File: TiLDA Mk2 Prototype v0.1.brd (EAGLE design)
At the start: 68 x 100 mm, 215 parts, among them IC1 ATSAM3X8EA-AU, IC2 MPU-6050, IC3 SRF-V1.2, IC4 LTC4160, IC5 S25FL216K0PMFI011, IC6 AT45DB161E-SSHFHA (NP), IC7 HMC5883LSMD (NP), IC8 MCP1825T-3302E/DC, J1 ZX62-AB-5PA(11), J2 FCI 62684-401100ALF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

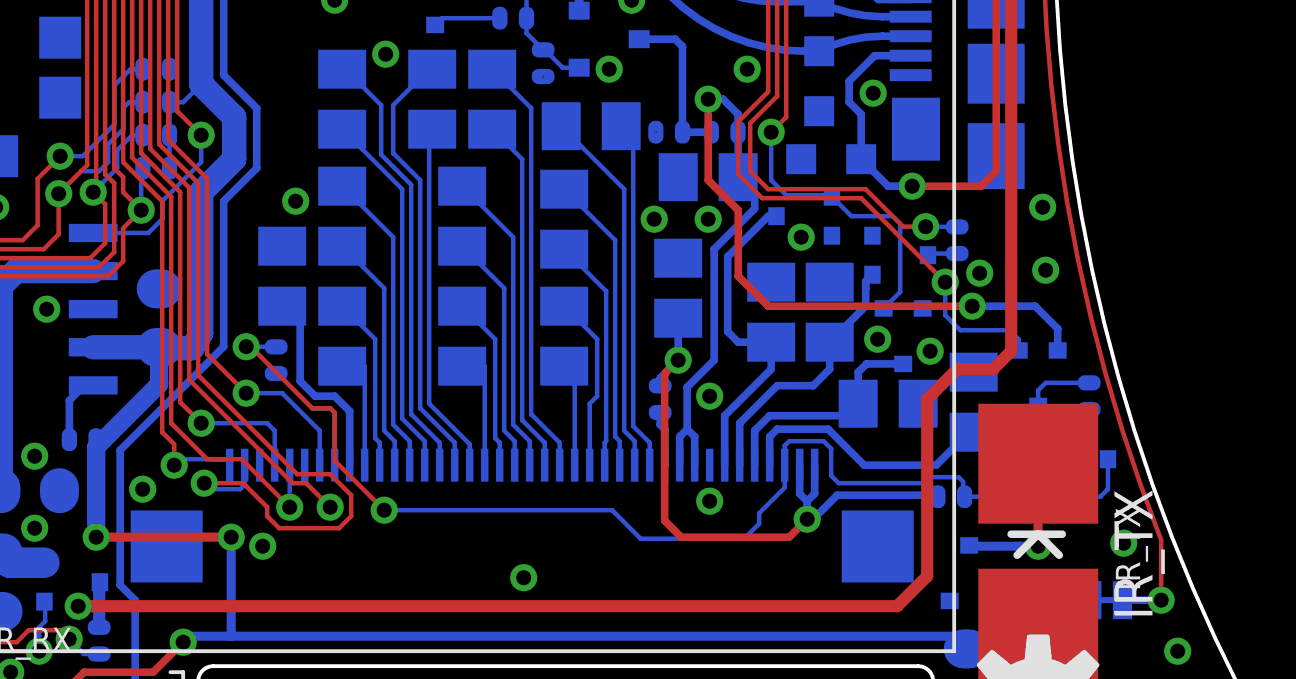
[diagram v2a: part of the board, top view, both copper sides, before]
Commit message: Prototype: C34, C38 to 10v, C21, C24, C25 to 0603 X5R
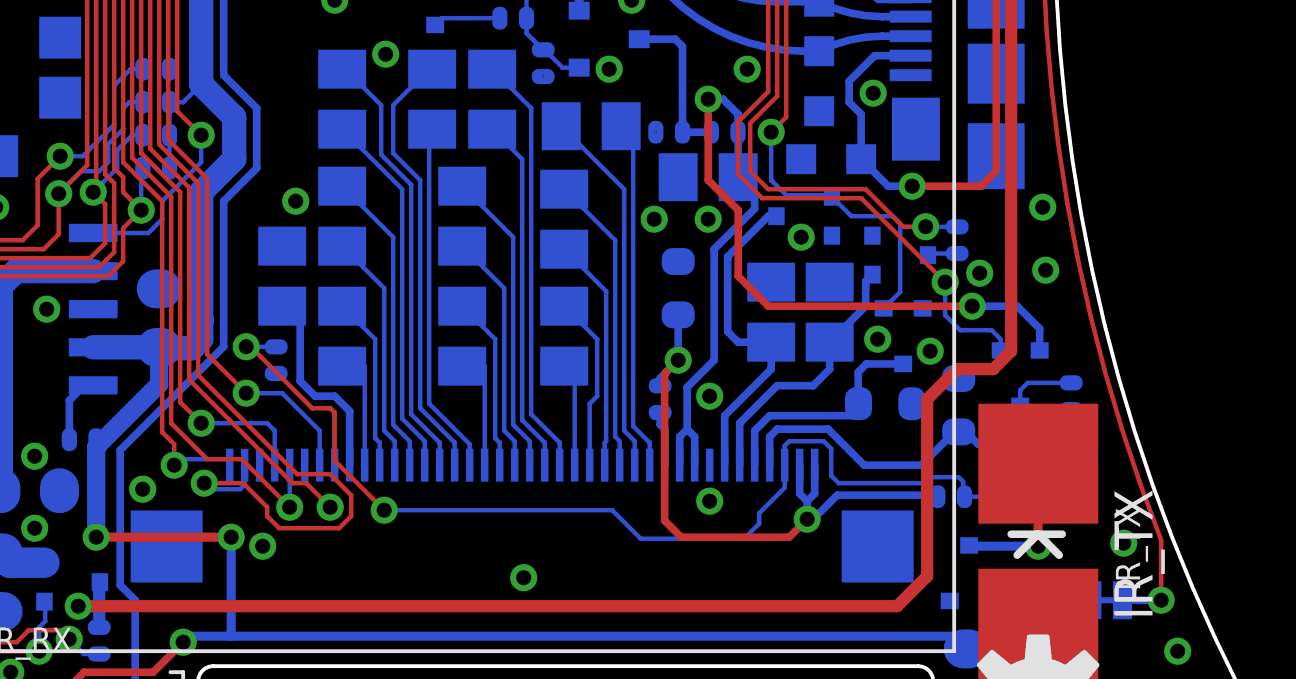
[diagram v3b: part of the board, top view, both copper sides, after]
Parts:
- C21, C24, C25: value 0805/1u/10V/X7R -> 0603/1u/10V/X5R; device TiLDA Mk2 Parts:C0805K -> TiLDA Mk2 Parts:C0603-ROUND
- C34, C38: value 0603/1u/6V/X5R -> 0603/1u/10V/X5R
- moved Q6 0.60 mm to (60.3, 10.9)
- moved Q7 0.60 mm to (58.9, 13.6)
- moved R10 0.60 mm to (58.4, 10.9)
- moved R12 0.60 mm to (60.6, 13.0)
- moved C25 0.51 mm to (56.9, 12.7)
- moved C24 0.10 mm to (54.4, 12.8)
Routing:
- net EPD_BORDER_CONTROL: track 65.8 -> 65.2 mm
- net EPD_VCC: track 33.9 -> 33.3 mm
- net BORDER: track 38.5 -> 37.9 mm
- net VDL: track 11.9 -> 11.3 mm

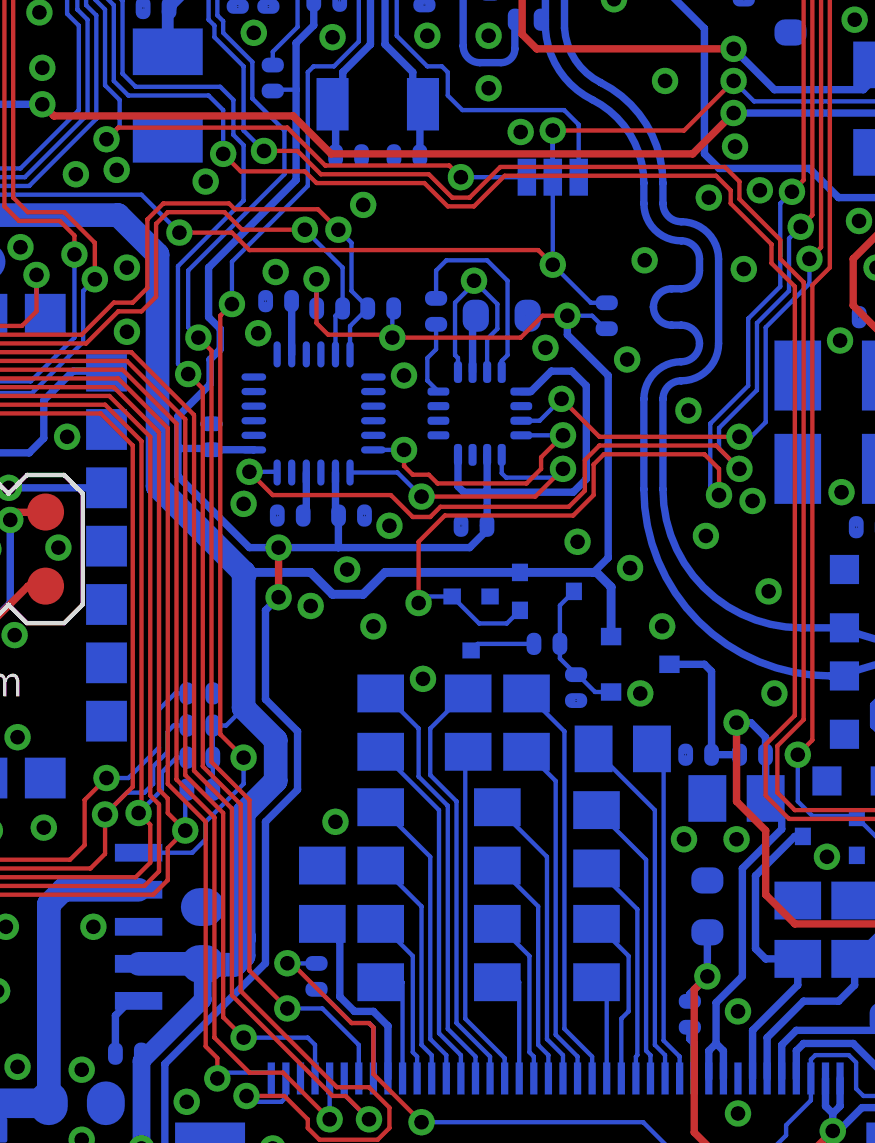
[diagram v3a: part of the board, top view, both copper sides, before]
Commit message: Prototype: Move C120 to NTRSB and VBackup
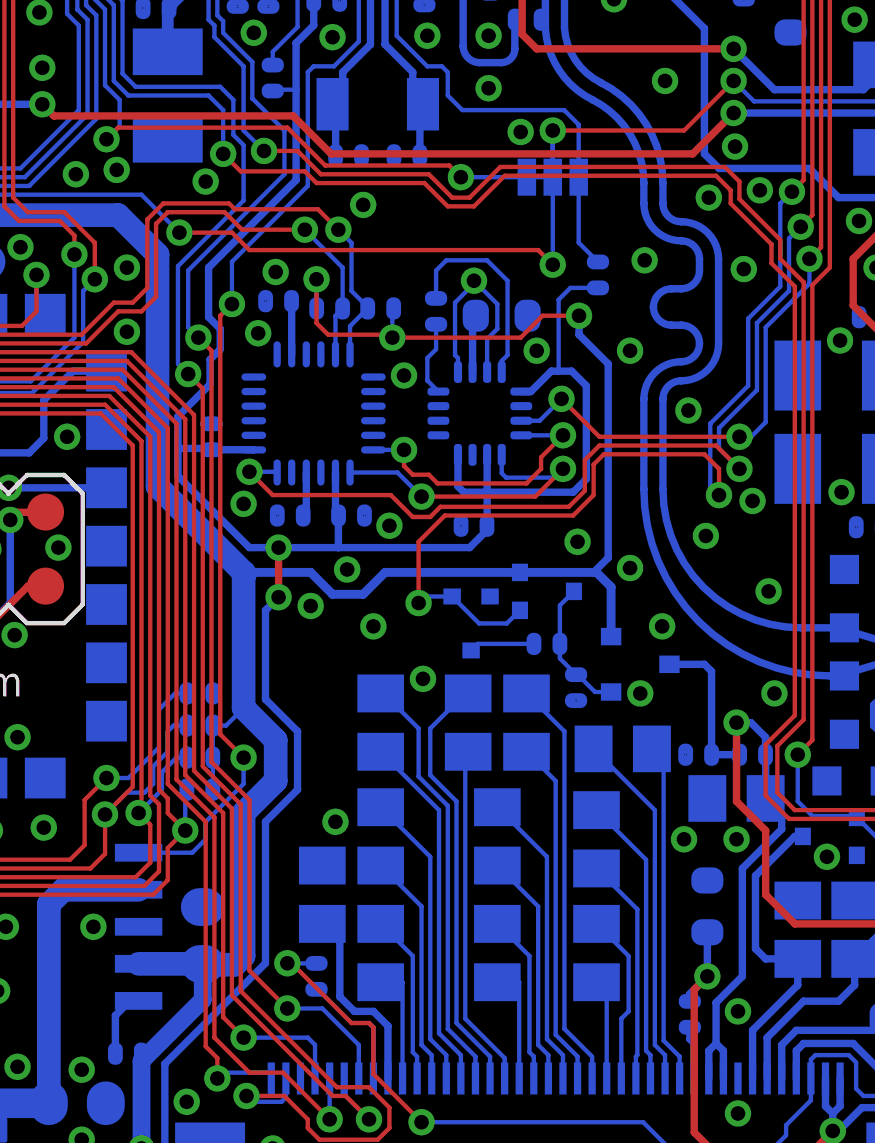
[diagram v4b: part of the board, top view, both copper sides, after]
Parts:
- moved C120 1.43 mm to (43.8, 38.2)
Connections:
- net 3V3: no longer C120.1
- net MASTER_RESET: no longer C120.2
- net NRSTB: now also C120.2
- net VBACKUP: now also C120.1
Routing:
- net VBACKUP: track 102.1 -> 106.1 mm
- net NRSTB: track 14.5 -> 17.6 mm
- net MASTER_RESET: track 165.0 -> 162.6 mm
- net 3V3: track 461.1 -> 459.5 mm
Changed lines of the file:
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@@
 <grid distance="0.1" unitdist="mm" unit="mm" style="lines" multiple="1" display="yes" altdistance="0.05" altunitdist="mm" altunit="mm"/>
 <layers>
-<layer number="1" name="Top" color="4" fill="1" visible="no" active="yes"/>
+<layer number="1" name="Top" color="4" fill="1" visible="yes" active="yes"/>
 <layer number="2" name="Route2" color="1" fill="3" visible="no" active="yes"/>
 <layer number="3" name="Route3" color="4" fill="3" visible="no" active="no"/>
@@
 <text x="40.2" y="28.3" size="0.6096" layer="22" ratio="15" rot="MR0">C27</text>
 <text x="41.4" y="37.7" size="0.6096" layer="22" ratio="15" rot="MR0">C28</text>
-<text x="44.7" y="35.9" size="0.6096" layer="22" ratio="15" rot="MR90">C120</text>
+<text x="44.4" y="37.2" size="0.6096" layer="22" ratio="15" rot="MR90">C120</text>
 <text x="37.9" y="38" size="0.6096" layer="22" ratio="15" rot="MR90">C31</text>
 <text x="37.2" y="38.6" size="0.6096" layer="22" ratio="15" rot="MR0">R33</text>
@@
 <element name="R8" library="TiLDA Mk2 Parts" package="R0402-ARDUINO-ROUND" value="0402/1K/5%" x="10.8" y="1" rot="MR180"/>
 <element name="R14" library="TiLDA Mk2 Parts" package="R0402-ARDUINO-ROUND" value="0402/1K/5%" x="12.55" y="1" rot="MR0"/>
-<element name="C120" library="TiLDA Mk2 Parts" package="C0402-ARDUINO-ROUND" value="0402/10n/10v/Y5V" x="44.05" y="36.85" rot="MR90"/>
+<element name="C120" library="TiLDA Mk2 Parts" package="C0402-ARDUINO-ROUND" value="0402/10n/10v/Y5V" x="43.75" y="38.25" rot="MR90"/>
 <element name="JP4" library="TiLDA Mk2 Parts" package="1X02_NO_SILK" value="DAC" x="9.64" y="81.63" rot="R270"/>
 <element name="JP5" library="TiLDA Mk2 Parts" package="1X02_NO_SILK" value="CAN" x="57.9" y="81.63" rot="R270"/>
@@
 <wire x1="32.6" y1="5" x2="31.2" y2="5" width="0.3048" layer="16"/>
 <wire x1="31.2" y1="5" x2="31" y2="4.8" width="0.3048" layer="16"/>
-<contactref element="C120" pad="1"/>
 <contactref element="R21" pad="2"/>
 <contactref element="R22" pad="2"/>
@@
 <wire x1="30.7" y1="14.6" x2="31.3" y2="14.6" width="0.8128" layer="16"/>
 <wire x1="31.3" y1="14.6" x2="31.6" y2="14.9" width="0.8128" layer="16"/>
-<wire x1="31.6" y1="14.9" x2="31.6" y2="15.6" width="0.8128" layer="16"/>
-<wire x1="31.6" y1="15.6" x2="31.6" y2="15.45" width="0.8128" layer="16"/>
-<wire x1="31.6" y1="15.45" x2="31.6" y2="19.8" width="0.8128" layer="16"/>
+<wire x1="31.6" y1="14.9" x2="31.6" y2="19.8" width="0.8128" layer="16"/>
 <wire x1="31.6" y1="19.8" x2="32.7" y2="20.9" width="0.8128" layer="16"/>
 <wire x1="32.7" y1="20.9" x2="32.7" y2="22.3" width="0.8128" layer="16"/>
@@
 <wire x1="5.73" y1="43.53" x2="4.8" y2="44.46" width="0.254" layer="16"/>
 <wire x1="19.95" y1="69.3055" x2="19.8555" y2="69.4" width="0.254" layer="16"/>
-<wire x1="44.05" y1="36.4055" x2="43.9945" y2="36.4055" width="0.15" layer="16"/>
-<wire x1="43.9945" y1="36.4055" x2="43.55" y2="36.85" width="0.15" layer="16"/>
-<wire x1="43.55" y1="36.85" x2="42.7055" y2="36.85" width="0.15" layer="16"/>
-<wire x1="42.7055" y1="36.85" x2="42.7" y2="36.8555" width="0.15" layer="16"/>
-<wire x1="42.7" y1="36.8555" x2="42.7" y2="36.85" width="0.15" layer="16"/>
-<wire x1="42.7" y1="36.85" x2="42.7" y2="36.2" width="0.254" layer="16"/>
-<wire x1="42.7" y1="36.2" x2="44.1" y2="34.8" width="0.254" layer="16"/>
-<wire x1="44.1" y1="34.8" x2="44.1" y2="28.55" width="0.254" layer="16"/>
+<wire x1="43.1" y1="36.85" x2="43.1" y2="36.2" width="0.254" layer="16"/>
+<wire x1="43.1" y1="36.2" x2="44.1" y2="35.2" width="0.254" layer="16"/>
+<wire x1="44.1" y1="35.2" x2="44.1" y2="28.55" width="0.254" layer="16"/>
 <wire x1="44.1" y1="28.55" x2="43.6" y2="28.05" width="0.254" layer="16"/>
-<via x="42.7" y="36.85" extent="1-16" drill="0.5"/>
+<via x="43.1" y="36.85" extent="1-16" drill="0.5"/>
 <wire x1="41.1" y1="36.1" x2="41.85" y2="36.85" width="0.15" layer="1"/>
-<wire x1="41.85" y1="36.85" x2="42.7" y2="36.85" width="0.15" layer="1"/>
+<wire x1="41.85" y1="36.85" x2="43.1" y2="36.85" width="0.15" layer="1"/>
 <wire x1="47.95" y1="65.65" x2="47.95" y2="65.75" width="0.4064" layer="1"/>
 <wire x1="47.95" y1="65.75" x2="48.2" y2="66" width="0.4064" layer="1"/>
@@
 <via x="48.45" y="42.65" extent="1-16" drill="0.5"/>
 <via x="36.05" y="26.2" extent="1-16" drill="0.5"/>
-<via x="41.95" y="35.75" extent="1-16" drill="0.5"/>
+<via x="41.65" y="35.65" extent="1-16" drill="0.5"/>
 <via x="54.6" y="41" extent="1-16" drill="0.5"/>
 <via x="53.3" y="38.5" extent="1-16" drill="0.5"/>
@@
 <via x="24.6" y="47.25" extent="1-16" drill="0.5"/>
 <via x="45.35" y="38.75" extent="1-16" drill="0.5"/>
-<via x="44.75" y="35.35" extent="1-16" drill="0.5"/>
+<via x="44.85" y="35.65" extent="1-16" drill="0.5"/>
 <via x="8.3" y="49.95" extent="1-16" drill="0.5"/>
 <via x="3.4" y="45.7" extent="1-16" drill="0.5"/>
@@
 <wire x1="42.589" y1="43.9" x2="39.1" y2="43.9" width="0.15" layer="16"/>
 <wire x1="39.1" y1="43.9" x2="38.6" y2="44.4" width="0.15" layer="16"/>
+<contactref element="C120" pad="2"/>
+<wire x1="43.089" y1="41.6" x2="43.089" y2="39.3555" width="0.15" layer="16"/>
+<wire x1="43.089" y1="39.3555" x2="43.75" y2="38.6945" width="0.15" layer="16"/>
 </signal>
 <signal name="AVREF">
@@
 <wire x1="11.05" y1="45.15" x2="10.56" y2="45.15" width="0.15" layer="16"/>
 <wire x1="10.56" y1="45.15" x2="9.64" y2="46.07" width="0.15" layer="16"/>
-<contactref element="C120" pad="2"/>
 <contactref element="SJ6" pad="1"/>
 <wire x1="60.3" y1="54.8" x2="60.6" y2="54.5" width="0.15" layer="16"/>
@@
 <wire x1="46.7" y1="43.2" x2="42.2" y2="43.2" width="0.15" layer="1"/>
 <wire x1="42.2" y1="43.2" x2="42.2" y2="38.6" width="0.15" layer="16"/>
-<wire x1="42.2" y1="38.6" x2="43.5055" y2="37.2945" width="0.15" layer="16"/>
-<wire x1="43.5055" y1="37.2945" x2="44.05" y2="37.2945" width="0.15" layer="16"/>
 <via x="42.2" y="43.2" extent="1-16" drill="0.5"/>
 <via x="48.4" y="44.9" extent="1-16" drill="0.5"/>
@@
 <wire x1="43.35" y1="31.25" x2="43.35" y2="34.45" width="0.254" layer="16"/>
 <wire x1="43.35" y1="34.45" x2="42.85" y2="34.95" width="0.254" layer="16"/>
-<wire x1="42.85" y1="34.95" x2="42.15" y2="34.95" width="0.254" layer="16"/>
+<wire x1="42.85" y1="34.95" x2="42.4" y2="34.95" width="0.254" layer="16"/>
+<wire x1="42.4" y1="34.95" x2="42.15" y2="34.95" width="0.254" layer="16"/>
 <wire x1="42.15" y1="34.95" x2="41.45" y2="34.25" width="0.254" layer="16"/>
 <wire x1="41.45" y1="34.25" x2="41.12" y2="34.25" width="0.254" layer="16"/>
@@
 <wire x1="32.6" y1="44.5555" x2="32.6445" y2="44.6" width="0.15" layer="16"/>
 <wire x1="32.6445" y1="44.6" x2="33.4" y2="44.6" width="0.15" layer="16"/>
+<contactref element="C120" pad="1"/>
+<wire x1="43.75" y1="37.8055" x2="42.8055" y2="37.8055" width="0.15" layer="16"/>
+<wire x1="42.8055" y1="37.8055" x2="42.4" y2="37.4" width="0.15" layer="16"/>
+<wire x1="42.4" y1="37.4" x2="42.4" y2="34.95" width="0.15" layer="16"/>
 </signal>
 <signal name="VBUS1">

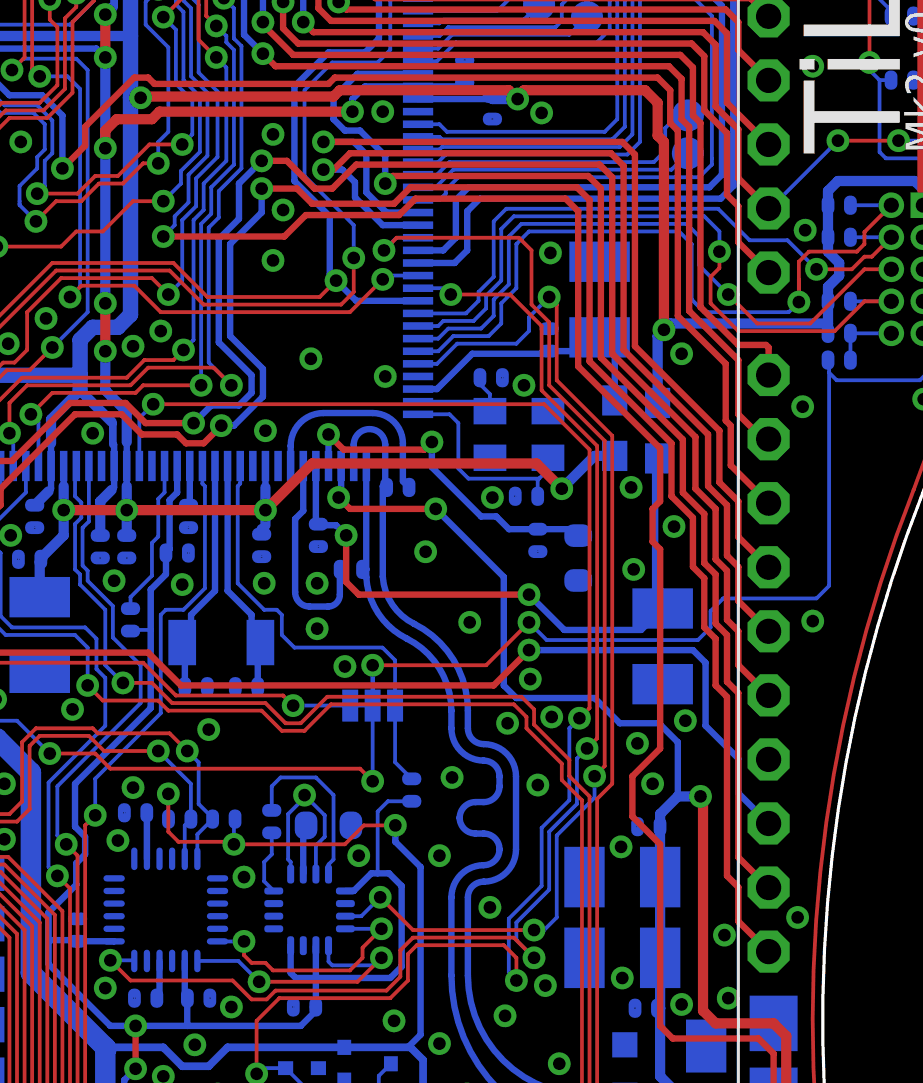
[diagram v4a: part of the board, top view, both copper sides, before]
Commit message: Prototype: Update for bigger X1 Crystal
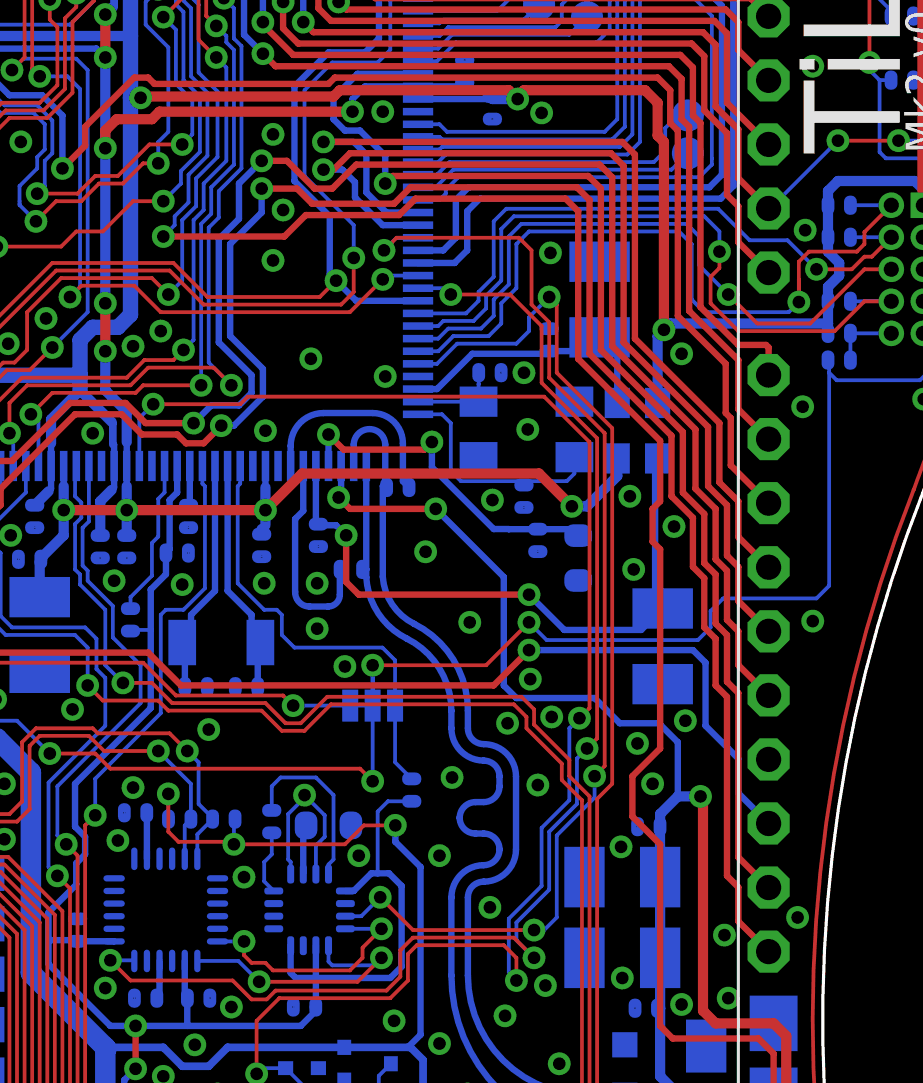
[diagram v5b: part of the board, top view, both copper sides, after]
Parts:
- C121, C122: value 0402/22p/ -> 0402/7p/
- C123, C124, C125: value 0402/22p/ -> 0402/15p/
- X1: value 12Mhz KX-7 20pF -> 12Mhz 13pF 30ppm (7pf caps); device TiLDA Mk2 Parts:CRYSTAL-3.2-2.5 -> TiLDA Mk2 Parts:CRYSTAL-5X3.2
- moved X1 0.36 mm to (48.3, 52.5)
- moved C121 0.21 mm to (46.9, 54.8)
- moved L105 0.14 mm to (51.9, 52.5)
- moved C122 0.10 mm to (48.2, 49.9), turned to 90 degrees
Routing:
- net XOUT: track 4.49 -> 3.63 mm
- net XIN: track 8.60 -> 9.34 mm
- net VDDOUT: track 86.4 -> 87.2 mm
- net GND: vias 235 -> 236
